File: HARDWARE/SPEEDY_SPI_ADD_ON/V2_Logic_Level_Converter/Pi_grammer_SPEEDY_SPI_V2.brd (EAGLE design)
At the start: 22.9 x 61 mm, 12 parts, among them J2 TARGET_copy

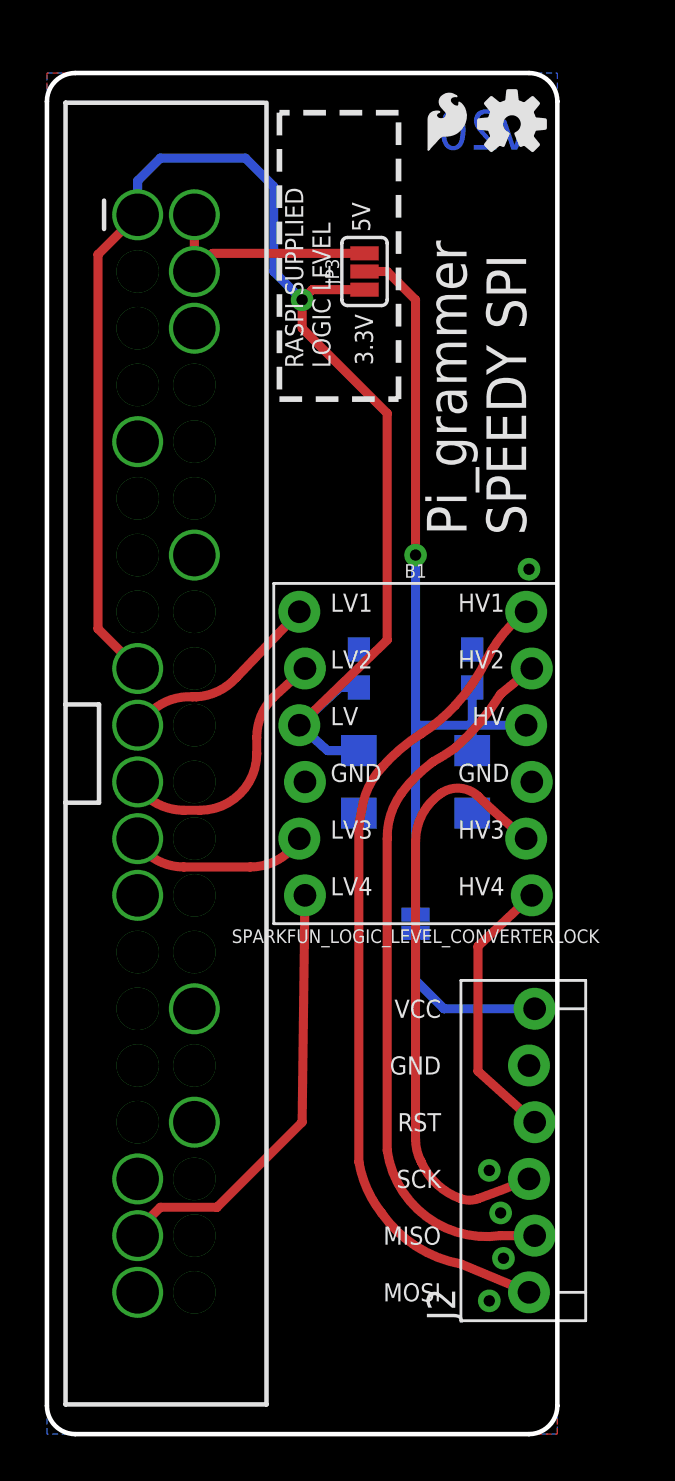
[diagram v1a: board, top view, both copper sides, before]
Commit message: Speedy SPI library work
updated device to only include pins/pads that are used. added in actual
drill hits for the unused pads.

rduced down to only 2 GND connections.

reduce isolate to 10 mils to allow for GND flow across header pins.
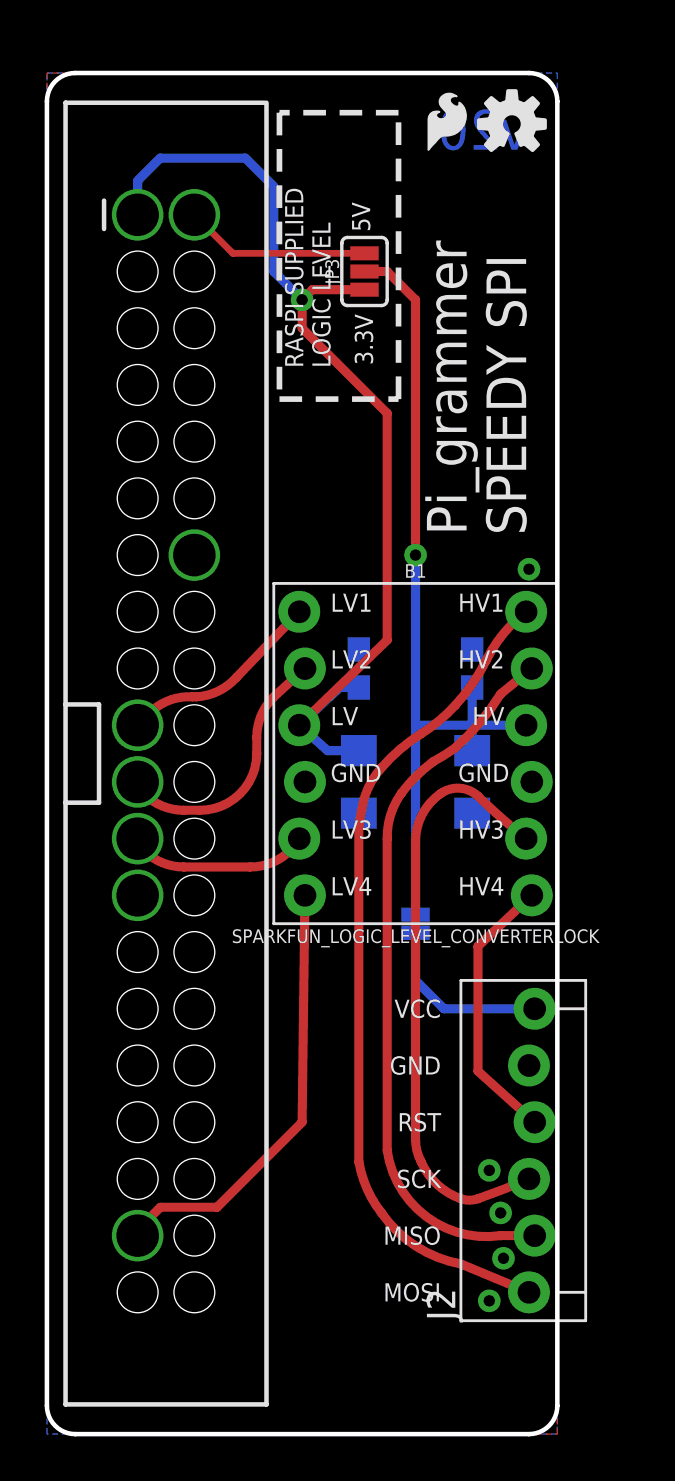
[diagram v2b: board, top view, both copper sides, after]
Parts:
- removed JP2: RASPBERRYPI-B+-GPIOSOLDER-ON-TOP, SparkFun-Boards:2X20-SHROUDED-SOLDER-ON-TOP
- added U$1: RASPIBERRYPI-B+-GPIO--SPECIAL, SparkFun-Boards:2X20-SHROUDED--SPECIAL
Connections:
- removed net CAPSENSE: JP2.33
- removed net CE0: JP2.24
- removed net CE1: JP2.26
- removed net FLASH_HEX_FAIL: JP2.11
- removed net FLASH_HEX_PASS: JP2.31
- removed net FUSE_BITS_FAIL: JP2.13
- removed net FUSE_BITS_PASS: JP2.15
- removed net GP20: JP2.38
- removed net GP21: JP2.40
- removed net ID_SC: JP2.28
- removed net ID_SD: JP2.27
- removed net LOCK_BITS_FAIL: JP2.22
- removed net LOCK_BITS_PASS: JP2.32
- removed net RXI: JP2.10
- removed net SCL: JP2.5
- removed net SCRIPT: JP2.7
- removed net SDA: JP2.3
- removed net SHUTDOWN: JP2.29
- removed net TXB_OE: JP2.35
- removed net TXO: JP2.8
- net 3.3V: now also U$1.1; no longer JP2.1, JP2.17
- net 5V: now also U$1.2; no longer JP2.2, JP2.4
- net GND: now also U$1.14, U$1.25; no longer JP2.14, JP2.20, JP2.25, JP2.30, JP2.34, JP2.39, JP2.6, JP2.9
- net MISO: now also U$1.21; no longer JP2.21
- net MOSI: now also U$1.19; no longer JP2.19
- net RST: now also U$1.37; no longer JP2.37
- net SCLK: now also U$1.23; no longer JP2.23
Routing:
- net 3.3V: track 67.7 -> 45.9 mm
- net 5V: track 10.5 -> 8.34 mm
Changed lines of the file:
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@@
 <layer number="47" name="Measures" color="7" fill="1" visible="no" active="yes"/>
 <layer number="48" name="Document" color="7" fill="1" visible="no" active="yes"/>
-<layer number="49" name="Reference" color="13" fill="1" visible="yes" active="yes"/>
+<layer number="49" name="Reference" color="13" fill="1" visible="no" active="yes"/>
 <layer number="50" name="dxf" color="7" fill="1" visible="no" active="yes"/>
 <layer number="51" name="tDocu" color="6" fill="1" visible="yes" active="yes"/>
@@
 <param name="mdDrill" value="8mil"/>
 <param name="mdSmdStop" value="0mil"/>
-<param name="msWidth" value="8mil"/>
+<param name="msWidth" value="10mil"/>
 <param name="msDrill" value="20mil"/>
 <param name="msMicroVia" value="9.99mm"/>
@@
 <param name="rvMicroViaOuter" value="0.25"/>
 <param name="rvMicroViaInner" value="0.25"/>
-<param name="rlMinPadTop" value="0mil"/>
+<param name="rlMinPadTop" value="8mil"/>
 <param name="rlMaxPadTop" value="20mil"/>
-<param name="rlMinPadInner" value="0mil"/>
+<param name="rlMinPadInner" value="8mil"/>
 <param name="rlMaxPadInner" value="20mil"/>
-<param name="rlMinPadBottom" value="0mil"/>
+<param name="rlMinPadBottom" value="8mil"/>
 <param name="rlMaxPadBottom" value="20mil"/>
-<param name="rlMinViaOuter" value="0mil"/>
+<param name="rlMinViaOuter" value="10mil"/>
 <param name="rlMaxViaOuter" value="20mil"/>
-<param name="rlMinViaInner" value="0mil"/>
+<param name="rlMinViaInner" value="10mil"/>
 <param name="rlMaxViaInner" value="20mil"/>
 <param name="rlMinMicroViaOuter" value="4mil"/>
@@
 <param name="checkFont" value="1"/>
 <param name="checkRestrict" value="1"/>
-<param name="useDiameter" value="15"/>
+<param name="useDiameter" value="13"/>
 <param name="maxErrors" value="50"/>
 </designrules>
@@
 </autorouter>
 <elements>
-<element name="JP2" library="SparkFun-Boards" package="2X20-SHROUDED-SOLDER-ON-TOP" value="RASPBERRYPI-B+-GPIOSOLDER-ON-TOP" x="49.784" y="45.72"/>
 <element name="LOGO1" library="SparkFun-Aesthetics" package="SFE_LOGO_FLAME_.1" value="SFE_LOGO_FLAME.1_INCH" x="61.214" y="72.39"/>
 <element name="LOGO2" library="SparkFun-Aesthetics" package="OSHW-LOGO-S" value="OSHW-LOGOS" x="65.278" y="73.914"/>
@@
 </element>
 <element name="JP1" library="SparkFun-Jumpers" package="SMT-JUMPER_2_NO_SILK" value="VCC_Target" x="60.96" y="38.1" rot="MR270"/>
+<element name="U$1" library="SparkFun-Boards" package="2X20-SHROUDED--SPECIAL" value="RASPIBERRYPI-B+-GPIO--SPECIAL" x="49.784" y="45.72"/>
 </elements>
 <signals>
-<signal name="SCL">
-<contactref element="JP2" pad="5"/>
-</signal>
-<signal name="SDA">
-<contactref element="JP2" pad="3"/>
-</signal>
 <signal name="GND">
-<contactref element="JP2" pad="9"/>
-<contactref element="JP2" pad="25"/>
-<contactref element="JP2" pad="14"/>
-<contactref element="JP2" pad="6"/>
-<contactref element="JP2" pad="30"/>
-<contactref element="JP2" pad="34"/>
-<contactref element="JP2" pad="39"/>
-<contactref element="JP2" pad="6"/>
-<contactref element="JP2" pad="9"/>
-<contactref element="JP2" pad="14"/>
-<contactref element="JP2" pad="25"/>
-<contactref element="JP2" pad="30"/>
-<contactref element="JP2" pad="34"/>
-<contactref element="JP2" pad="39"/>
 <contactref element="J2" pad="5"/>
-<polygon width="0.2032" layer="16" isolate="0.3048">
+<polygon width="0.2032" layer="16" isolate="0.254">
 <vertex x="44.45" y="76.2"/>
 <vertex x="67.31" y="76.2"/>
@@
 <vertex x="44.45" y="15.24"/>
 </polygon>
-<polygon width="0.2032" layer="1" isolate="0.3048">
+<polygon width="0.2032" layer="1" isolate="0.254">
 <vertex x="44.45" y="76.2"/>
 <vertex x="44.45" y="16.51" curve="90"/>
@@
 <via x="64.262" y="21.209" extent="1-16" drill="0.508" diameter="1.016"/>
 <via x="66.04" y="53.975" extent="1-16" drill="0.508" diameter="1.016"/>
-<contactref element="JP2" pad="20"/>
+<contactref element="U$1" pad="14"/>
+<contactref element="U$1" pad="25"/>
 </signal>
 <signal name="5V">
-<contactref element="JP2" pad="2"/>
-<contactref element="JP2" pad="2"/>
 <contactref element="JP3" pad="3"/>
-<wire x1="51.054" y1="67.31" x2="51.8668" y2="68.1228" width="0.4064" layer="1"/>
-<wire x1="51.8668" y1="68.1228" x2="58.674" y2="68.1228" width="0.4064" layer="1"/>
-<wire x1="51.054" y1="67.31" x2="51.054" y2="69.85" width="0.4064" layer="1"/>
-<contactref element="JP2" pad="4"/>
+<contactref element="U$1" pad="2"/>
+<wire x1="58.674" y1="68.1228" x2="52.7812" y2="68.1228" width="0.3048" layer="1"/>
+<wire x1="52.7812" y1="68.1228" x2="51.054" y2="69.85" width="0.3048" layer="1"/>
 </signal>
 <signal name="3.3V">
-<contactref element="JP2" pad="1"/>
-<contactref element="JP2" pad="1"/>
 <contactref element="JP3" pad="1"/>
 <contactref element="B1" pad="LV"/>
@@
 <wire x1="55.88" y1="64.77" x2="59.69" y2="60.96" width="0.4064" layer="1"/>
 <wire x1="59.69" y1="60.96" x2="59.69" y2="50.8" width="0.4064" layer="1"/>
-<wire x1="46.736" y1="51.308" x2="46.736" y2="68.072" width="0.4064" layer="1"/>
 <wire x1="55.753" y1="46.99" x2="59.69" y2="50.8" width="0.4064" layer="1"/>
-<wire x1="46.736" y1="68.072" x2="48.514" y2="69.85" width="0.4064" layer="1"/>
-<wire x1="46.736" y1="51.308" x2="48.514" y2="49.53" width="0.4064" layer="1"/>
-<contactref element="JP2" pad="17"/>
-</signal>
-<signal name="TXO">
-<contactref element="JP2" pad="8"/>
-</signal>
-<signal name="RXI">
-<contactref element="JP2" pad="10"/>
+<contactref element="U$1" pad="1"/>
 </signal>
 <signal name="SCK_T">
@@
 <wire x1="62.738" y1="45.974" x2="64.77" y2="48.387" width="0.4064" layer="1" curve="16.535472"/>
 </signal>
-<signal name="ID_SD">
-<contactref element="JP2" pad="27"/>
-</signal>
-<signal name="ID_SC">
-<contactref element="JP2" pad="28"/>
-</signal>
 <signal name="MOSI">
-<contactref element="JP2" pad="19"/>
 <contactref element="B1" pad="LV1"/>
 <wire x1="48.514" y1="46.99" x2="49.16705" y2="47.64305" width="0.4064" layer="1"/>
@@
 <wire x1="51.144896875" y1="48.26" x2="52.94095" y2="49.13095" width="0.4064" layer="1" curve="45.00005"/>
 <wire x1="52.94095" y1="49.13095" x2="55.753" y2="52.07" width="0.4064" layer="1"/>
-</signal>
-<signal name="CE0">
-<contactref element="JP2" pad="24"/>
-</signal>
-<signal name="CE1">
-<contactref element="JP2" pad="26"/>
+<contactref element="U$1" pad="19"/>
 </signal>
 <signal name="RST_T">
@@
 <wire x1="63.754" y1="31.496" x2="66.294" y2="29.21" width="0.4064" layer="1"/>
 </signal>
-<signal name="GP20">
-<contactref element="JP2" pad="38"/>
-</signal>
-<signal name="GP21">
-<contactref element="JP2" pad="40"/>
-</signal>
 <signal name="RST">
-<contactref element="JP2" pad="37"/>
 <contactref element="B1" pad="LV4"/>
 <wire x1="48.514" y1="24.13" x2="48.514" y2="24.384" width="0.4064" layer="1"/>
@@
 <wire x1="52.07" y1="25.4" x2="55.88" y2="29.21" width="0.4064" layer="1"/>
 <wire x1="55.88" y1="29.21" x2="56.007" y2="39.37" width="0.4064" layer="1"/>
+<contactref element="U$1" pad="37"/>
 </signal>
 <signal name="SCLK">
-<contactref element="JP2" pad="23"/>
 <contactref element="B1" pad="LV3"/>
 <wire x1="48.514" y1="41.91" x2="48.514" y2="41.656" width="0.4064" layer="1"/>
@@
 <wire x1="53.557896875" y1="40.64" x2="55.35395" y2="41.38395" width="0.4064" layer="1" curve="45.00005"/>
 <wire x1="55.35395" y1="41.38395" x2="55.753" y2="41.91" width="0.4064" layer="1"/>
+<contactref element="U$1" pad="23"/>
 </signal>
 <signal name="MISO">
-<contactref element="JP2" pad="21"/>
 <contactref element="B1" pad="LV2"/>
 <wire x1="48.514" y1="44.45" x2="48.514" y2="44.196" width="0.4064" layer="1"/>
@@
 <wire x1="56.007" y1="49.53" x2="54.59195" y2="48.24195" width="0.4064" layer="1"/>
 <wire x1="54.59195" y1="48.24195" x2="53.848" y2="46.445896875" width="0.4064" layer="1" curve="45.00007"/>
-</signal>
-<signal name="FLASH_HEX_FAIL">
-<contactref element="JP2" pad="11"/>
-</signal>
-<signal name="FUSE_BITS_FAIL">
-<contactref element="JP2" pad="13"/>
-</signal>
-<signal name="FUSE_BITS_PASS">
-<contactref element="JP2" pad="15"/>
-</signal>
-<signal name="SCRIPT">
-<contactref element="JP2" pad="7"/>
+<contactref element="U$1" pad="21"/>
 </signal>
 <signal name="MOSI_T">
@@
 <wire x1="64.135" y1="49.911" x2="65.913" y2="52.07" width="0.4064" layer="1" curve="-26.558078"/>
 </signal>
-<signal name="FLASH_HEX_PASS">
-<contactref element="JP2" pad="31"/>
-</signal>
-<signal name="SHUTDOWN">
-<contactref element="JP2" pad="29"/>
-</signal>
-<signal name="LOCK_BITS_PASS">
-<contactref element="JP2" pad="32"/>
-</signal>
-<signal name="CAPSENSE">
-<contactref element="JP2" pad="33"/>
-</signal>
-<signal name="LOCK_BITS_FAIL">
-<contactref element="JP2" pad="22"/>
-</signal>
-<signal name="TXB_OE">
-<contactref element="JP2" pad="35"/>
-</signal>
 <signal name="N$4">

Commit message: moved 1x6 header to allow for RA header
This should allow for the cable to flow directly downward from the
pi_grammer and sit with a lower profile. This should help prevent the
cable/header from getting knocked around during handling.

Also had to update the adapter - rotated header 180 degrees so it will
mate straight pin-to-pin on the 1x6 header on the speedySPI.
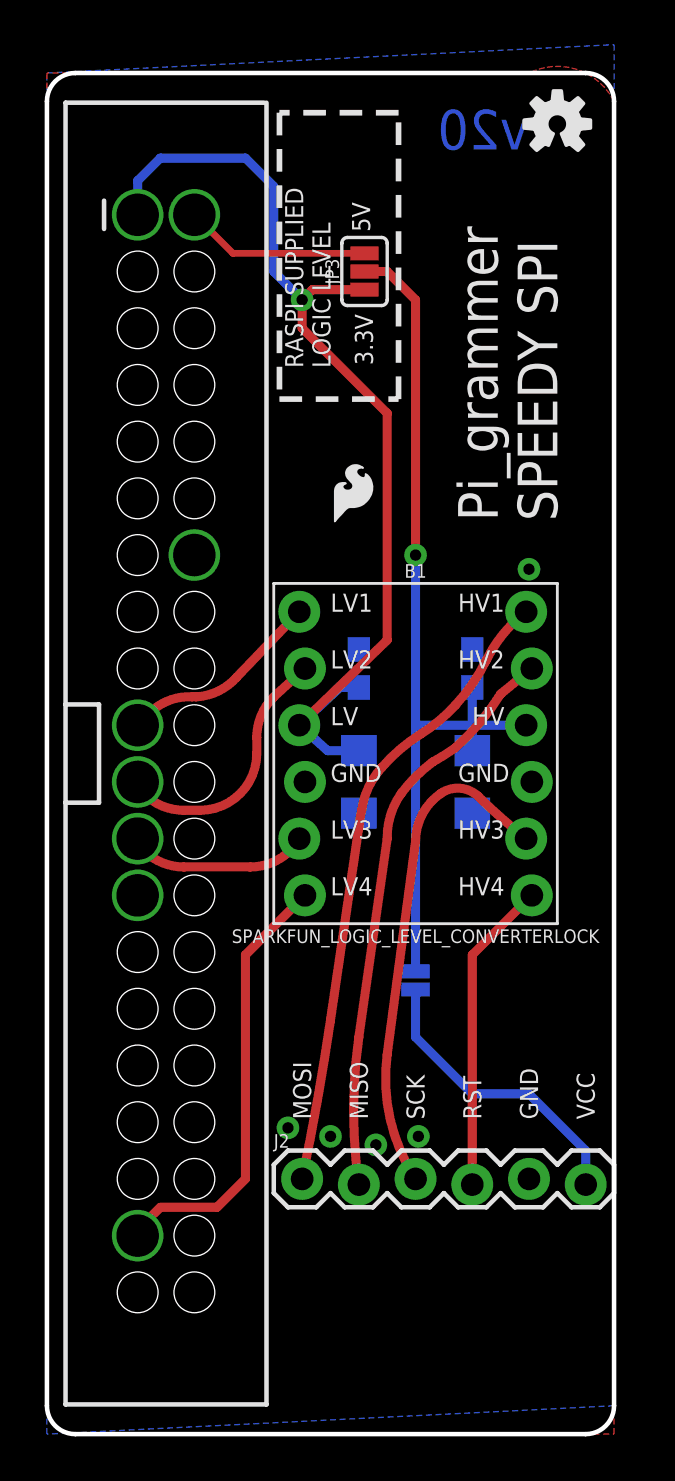
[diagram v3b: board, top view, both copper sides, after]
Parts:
- J2: device SparkFun-Connectors:MOLEX-1X6_LOCK -> SparkFun-Connectors:1X06-SIP_LOCK
- moved LOGO1 17.2 mm to (57.0, 55.8)
- moved J2 11.4 mm to (55.9, 26.7), turned to 0 degrees
- moved JP1 2.54 mm to (61.0, 35.6)
- moved LOGO2 2.03 mm to (67.3, 73.9)
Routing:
- net MOSI_T: track 37.5 -> 28.4 mm
- net MISO_T: track 32.1 -> 25.8 mm
- net VCC_T: track 7.99 -> 13.4 mm
- net SCK_T: track 27.0 -> 22.3 mm
- net N$4: track 38.1 -> 40.7 mm
- net RST_T: track 12.3 -> 14.1 mm
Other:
- board size 22.9 x 61 mm -> 25.4 x 61 mm
